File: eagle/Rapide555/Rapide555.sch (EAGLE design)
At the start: 15 parts, among them IC1 555, Q1 IRLZ44Z

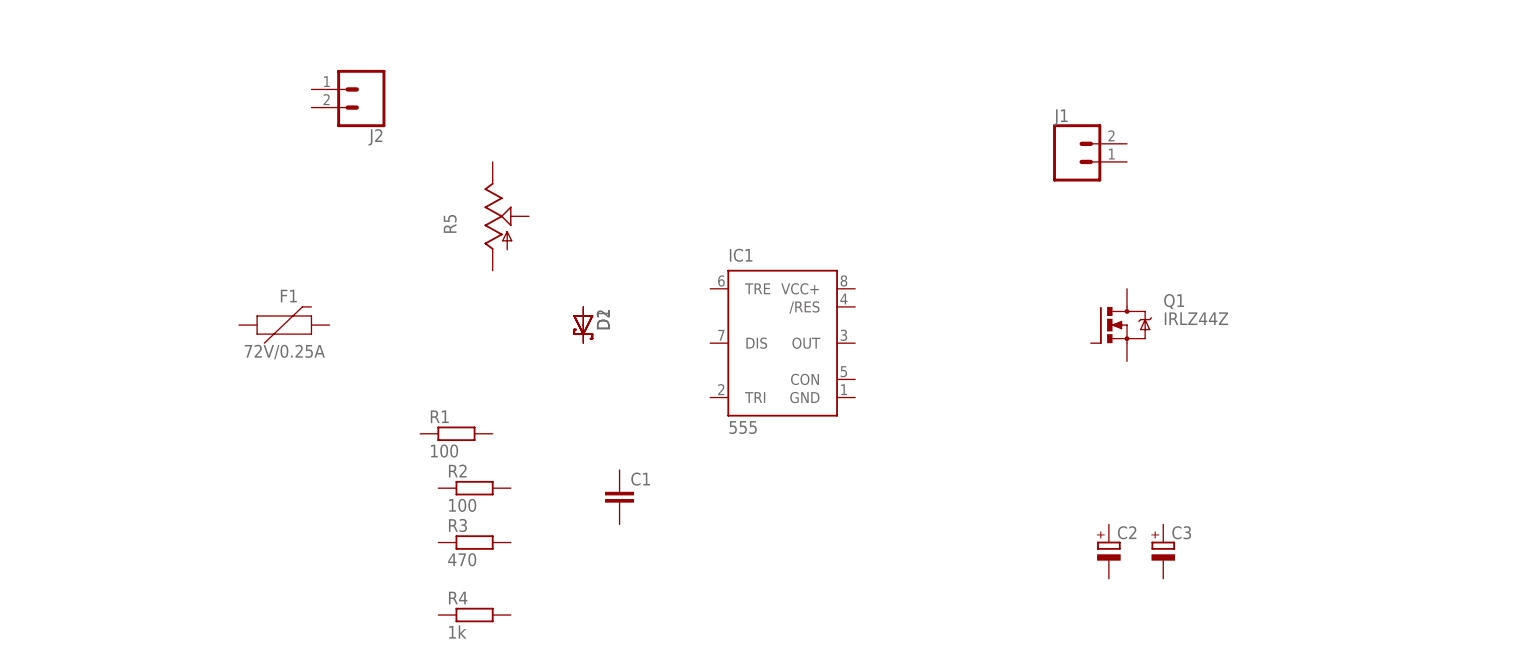
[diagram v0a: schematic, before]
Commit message: Added brd for Rapide555 (still WIP)
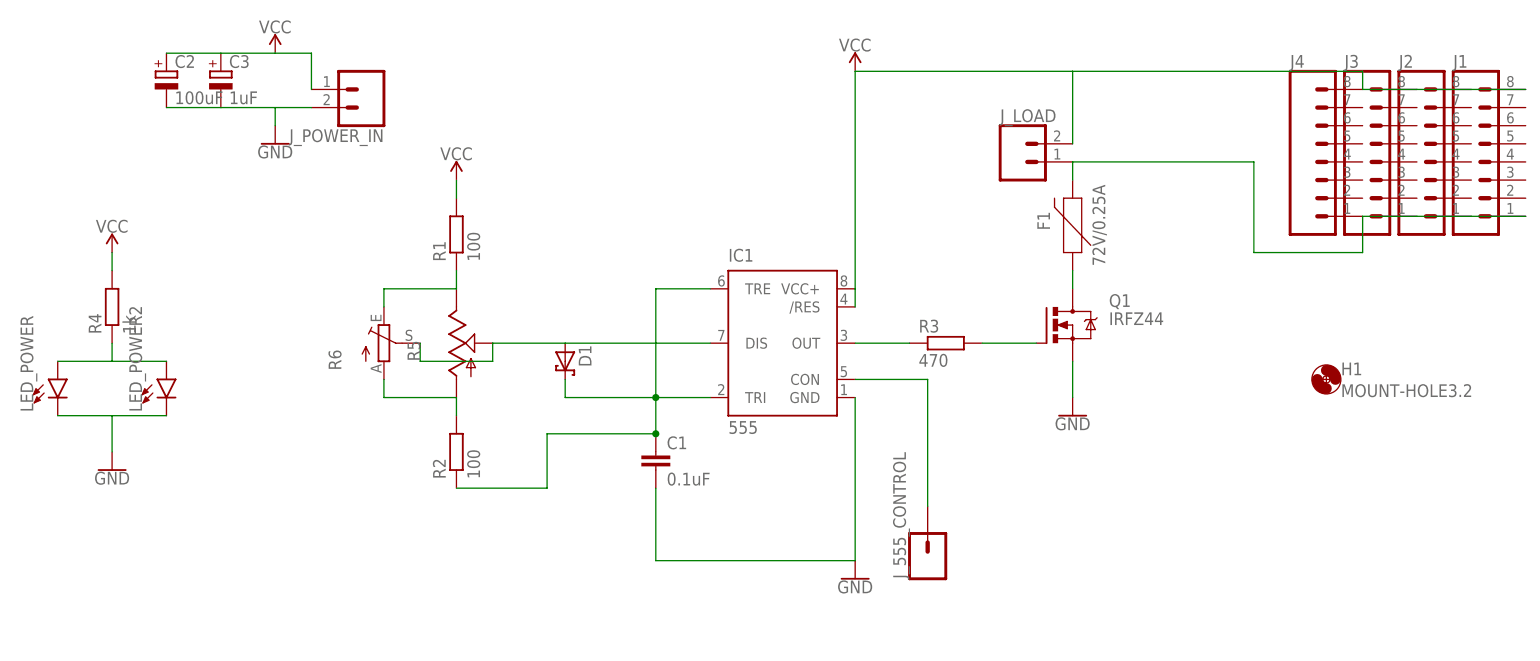
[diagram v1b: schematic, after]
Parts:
- removed D2: (no value), diode:SCHOTTKY-DIODEDO35-7
- added H1: MOUNT-HOLE3.2, holes:MOUNT-HOLE3.2
- added J3, J4: (no value), SparkFun-Connectors:CONN_08NO_SILK_FEMALE_PTH
- added J_555_CONTROL: (no value), SparkFun-Connectors:CONN_01
- added J_LOAD, J_POWER_IN: (no value), SparkFun-Connectors:CONN_023.5MM
- added LED_POWER: (no value), SparkFun-LED:LED3MM
- added LED_POWER2: (no value), SparkFun-LED:LED-FKIT-1206
- added R6: (no value), pot:TRIM_EU-B25P
- C1: value (none) -> 0.1uF
- C2: value (none) -> 100uF
- C3: value (none) -> 1uF; device resistor:CPOL-EUE5-8.5 -> resistor:CPOL-EUE2,5-6E
- J1, J2: device SparkFun-Connectors:CONN_023.5MM -> SparkFun-Connectors:CONN_08NO_SILK_FEMALE_PTH
- Q1: value IRLZ44Z -> IRFZ44; device transistor-power:IRLZ44Z -> transistor-power:IXFH6N90
- R1, R3: device resistor:R-EU_0204/2V -> resistor:R-EU_0204/5
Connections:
- new net GND: C1.2, C2.-, C3.-, IC1.GND, J_POWER_IN.2, LED_POWER.C, LED_POWER2.C, Q1.S
- new net N$12: LED_POWER.A, LED_POWER2.A, R4.1
- new net N$3: F1.1, Q1.D
- new net N$4: IC1.CON, J_555_CONTROL.1
- new net N$5: IC1.OUT, R3.1
- new net N$6: Q1.G, R3.2
- new net N$7: C1.1, D1.C, IC1.TRE, IC1.TRI, R2.1
- new net N$8: R1.1, R5.E, R6.E
- new net N$9: R2.2, R5.A, R6.A
- new net VCC: C2.+, C3.+, IC1./RES, IC1.VCC+, J1.8, J2.8, J3.8, J4.8, J_LOAD.2, J_POWER_IN.1, R1.2, R4.2
- net N$1: now also IC1.DIS, R5.S, R6.S; no longer D2.A
- net N$2: now also F1.2, J1.1, J2.1, J3.1, J4.1, J_LOAD.1; no longer D1.C, D2.C
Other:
- moved on the sheet: C1, C2, C3, D1, F1, Q1, R1, R2, R3, R4, R5

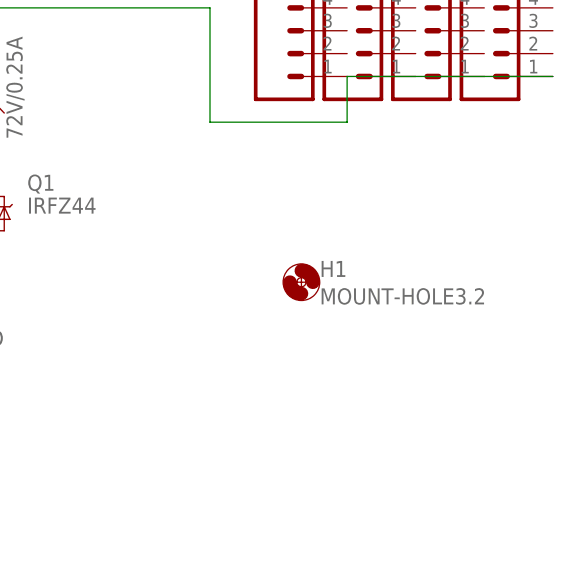
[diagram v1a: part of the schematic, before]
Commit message: Rapide555 board beta ok, need labels and review.
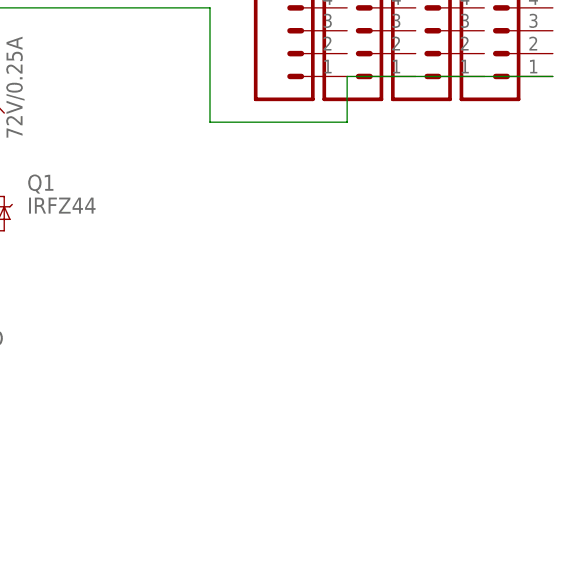
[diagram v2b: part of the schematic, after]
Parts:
- removed H1: MOUNT-HOLE3.2, holes:MOUNT-HOLE3.2
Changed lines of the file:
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@@
 <part name="J3" library="SparkFun-Connectors" deviceset="CONN_08" device="NO_SILK_FEMALE_PTH"/>
 <part name="J4" library="SparkFun-Connectors" deviceset="CONN_08" device="NO_SILK_FEMALE_PTH"/>
-<part name="H1" library="holes" deviceset="MOUNT-HOLE" device="3.2"/>
 </parts>
 <sheets>
@@
 <instance part="J3" gate="G$1" x="132.08" y="73.66"/>
 <instance part="J4" gate="G$1" x="124.46" y="73.66"/>
-<instance part="H1" gate="G$1" x="124.46" y="43.18"/>
 </instances>
 <busses>

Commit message: Added labels, ready for production
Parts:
- removed R5: (no value), pot:TRIM_US-CA14H
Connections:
- net N$1: no longer R5.S
- net N$8: no longer R5.E
- net N$9: no longer R5.A
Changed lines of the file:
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@@
 <?xml version="1.0" encoding="utf-8"?>
 <!DOCTYPE eagle SYSTEM "eagle.dtd">
-<eagle version="6.5.0">
+<eagle version="7.7.0">
 <drawing>
 <settings>
@@
 <part name="R3" library="resistor" deviceset="R-EU_" device="0204/5" value="470"/>
 <part name="R4" library="resistor" deviceset="R-EU_" device="0204/2V" value="1k"/>
-<part name="R5" library="pot" deviceset="TRIM_US-" device="CA14H"/>
 <part name="D1" library="diode" deviceset="SCHOTTKY-DIODE" device="DO35-7"/>
 <part name="Q1" library="transistor-power" deviceset="IXF?6N*" device="H" technology="90" value="IRFZ44"/>
@@
 <instance part="R3" gate="G$1" x="71.12" y="48.26"/>
 <instance part="R4" gate="G$1" x="-45.72" y="53.34" rot="R90"/>
-<instance part="R5" gate="G$1" x="2.54" y="48.26"/>
 <instance part="D1" gate="G$1" x="17.78" y="45.72" rot="R270"/>
 <instance part="Q1" gate="G$1" x="86.36" y="50.8"/>
@@
 <pinref part="D1" gate="G$1" pin="A"/>
 <wire x1="38.1" y1="48.26" x2="17.78" y2="48.26" width="0.1524" layer="91"/>
-<pinref part="R5" gate="G$1" pin="S"/>
 <wire x1="7.62" y1="48.26" x2="17.78" y2="48.26" width="0.1524" layer="91"/>
 <pinref part="R6" gate="1" pin="S"/>
@@
 <segment>
 <pinref part="R1" gate="G$1" pin="1"/>
-<pinref part="R5" gate="G$1" pin="E"/>
 <wire x1="2.54" y1="58.42" x2="2.54" y2="55.88" width="0.1524" layer="91"/>
 <pinref part="R6" gate="1" pin="E"/>
@@
 <net name="N$9" class="0">
 <segment>
-<pinref part="R5" gate="G$1" pin="A"/>
 <pinref part="R2" gate="G$1" pin="2"/>
 <wire x1="2.54" y1="40.64" x2="2.54" y2="38.1" width="0.1524" layer="91"/>
